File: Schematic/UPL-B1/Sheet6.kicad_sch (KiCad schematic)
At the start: 3 parts, among them X1 5102159-8, X3 Conn_01x06_Pin, X4 Conn_01x06_Pin

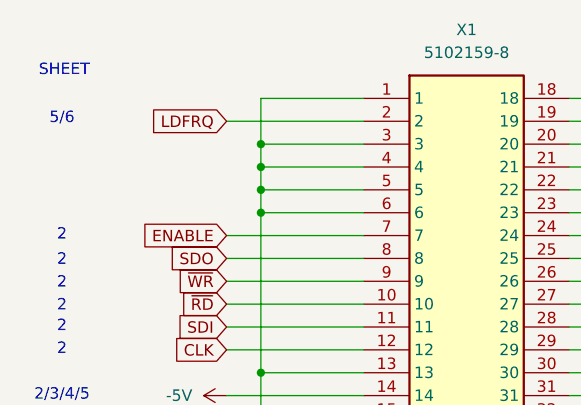
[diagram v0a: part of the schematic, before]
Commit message: Added Integrator 1 and Level control
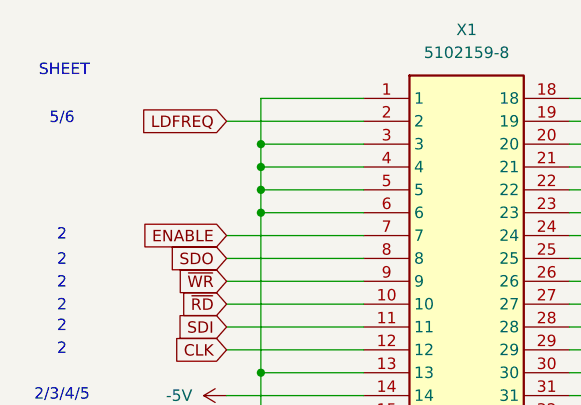
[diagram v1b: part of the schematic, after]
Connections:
- net LDFRQ renamed LDFREQ

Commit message: updated to hierarchical labels
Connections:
- net LOW DIST renamed LOW_DIST
